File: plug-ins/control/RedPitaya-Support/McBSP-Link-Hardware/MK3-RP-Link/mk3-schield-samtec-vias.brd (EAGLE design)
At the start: 59.4 x 51.2 mm, 16 parts, among them U1 SN65MLVD202A, U2 SN65MLVD202A, U3 SN65MLVD202A

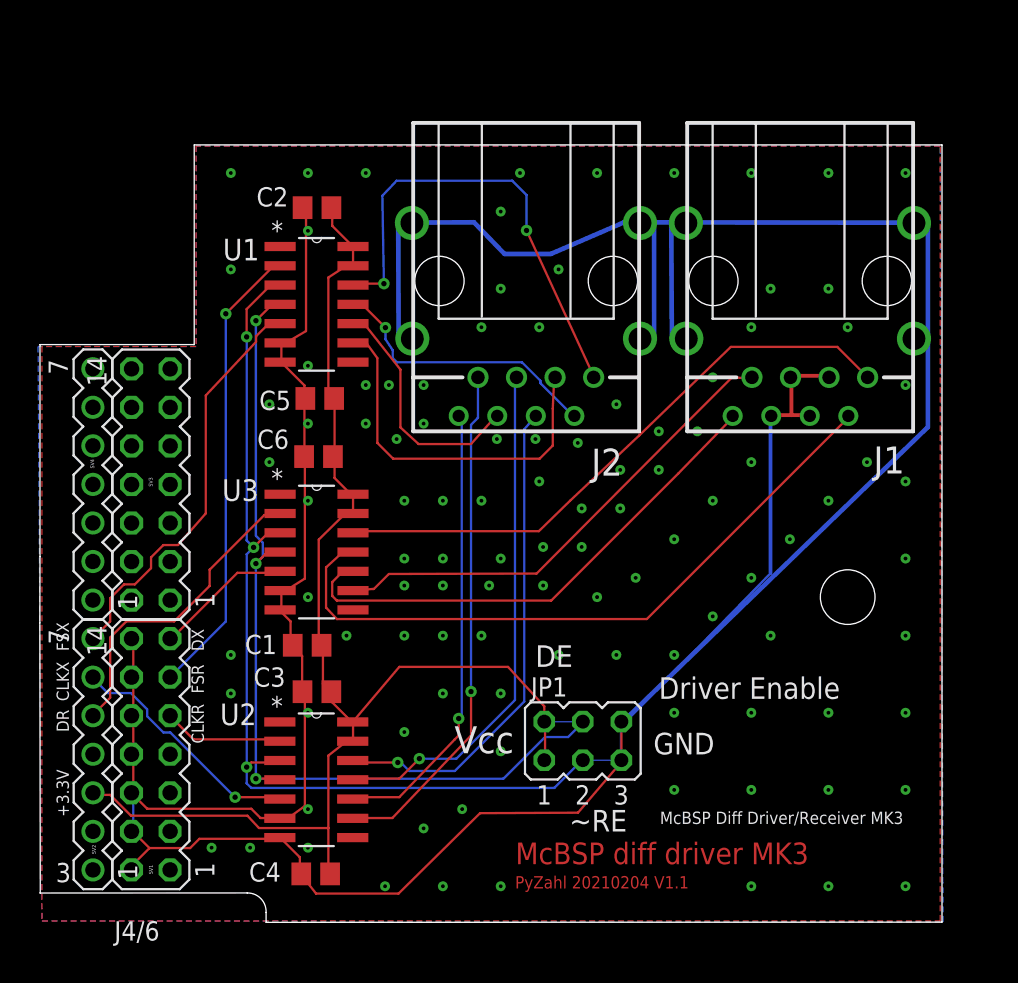
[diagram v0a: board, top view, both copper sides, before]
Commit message: added next version and support material
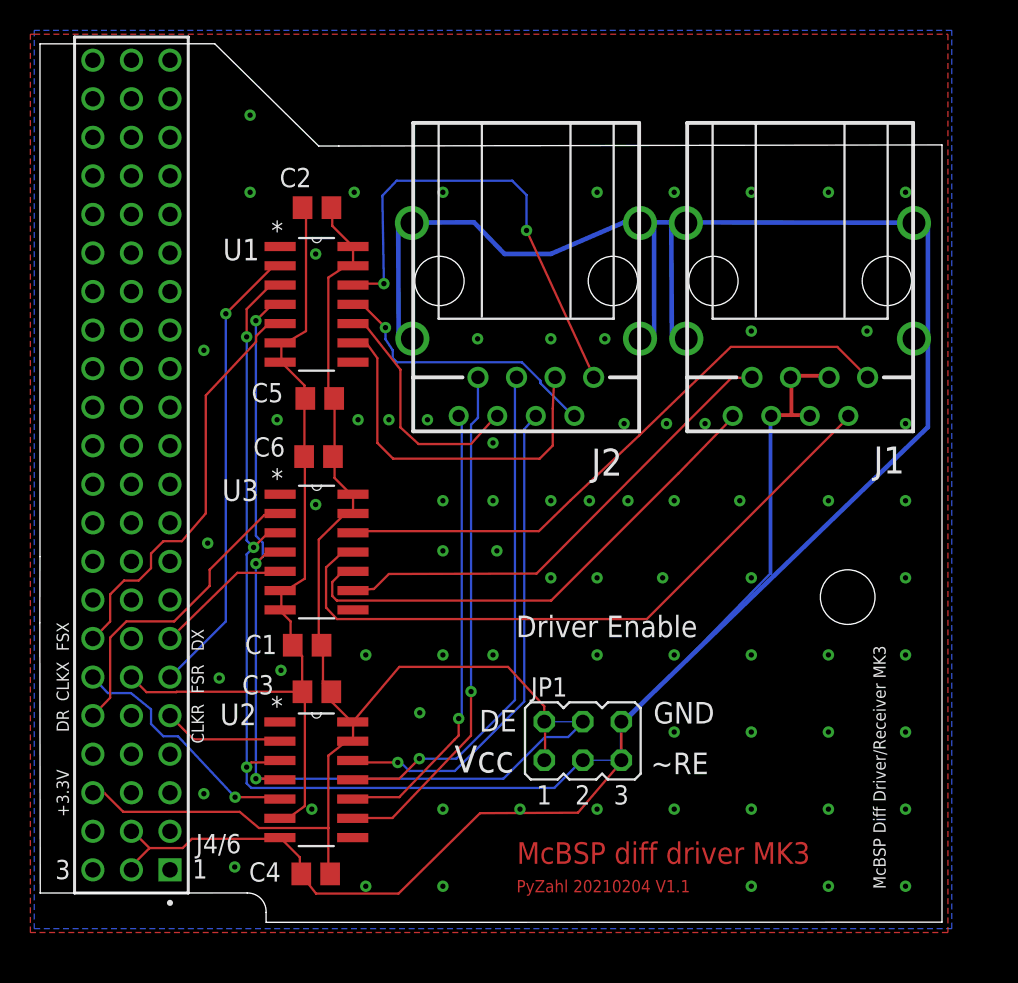
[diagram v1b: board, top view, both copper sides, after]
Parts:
- removed SV1, SV3: J4, con-lstb:MA07-2
- removed SV2, SV4: (no value), con-lstb-copy:MA07-1
- added J4/6: ESQ-122-13-L-T, ESQ-122-13-L-T:SAMTEC_ESQ-122-13-L-T
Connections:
- net CLKR0: now also J4/6.13; no longer SV1.9
- net CLKX0: now also J4/6.18; no longer SV2.6
- net DR0: now also J4/6.15; no longer SV2.5
- net DX0: now also J4/6.19; no longer SV1.13
- net FSR0: now also J4/6.16; no longer SV1.11
- net FSX0: now also J4/6.21; no longer SV2.7
- net GND: now also J4/6.02, J4/6.05, J4/6.08, J4/6.11, J4/6.14, J4/6.17, J4/6.20, J4/6.23, J4/6.26, J4/6.29, J4/6.32, J4/6.35, J4/6.38, J4/6.41, J4/6.44, J4/6.47, J4/6.50, J4/6.53, J4/6.56, J4/6.59, J4/6.62, J4/6.65; no longer SV1.10, SV1.12, SV1.14, SV1.2, SV1.4, SV1.6, SV1.8
- net VCC+3.3V: now also J4/6.09; no longer SV2.3
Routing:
- net GND: track 253.3 -> 241.0 mm, vias 0 -> 73
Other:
- board size 59.4 x 51.2 mm -> 59.4 x 57.9 mm
- board text added: "1"
- board text removed: "J4/6"

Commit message: updated McBSP Link board/schematics updated FPGA bit file for (latest build for V2 Hardware/Interface), design cleanups
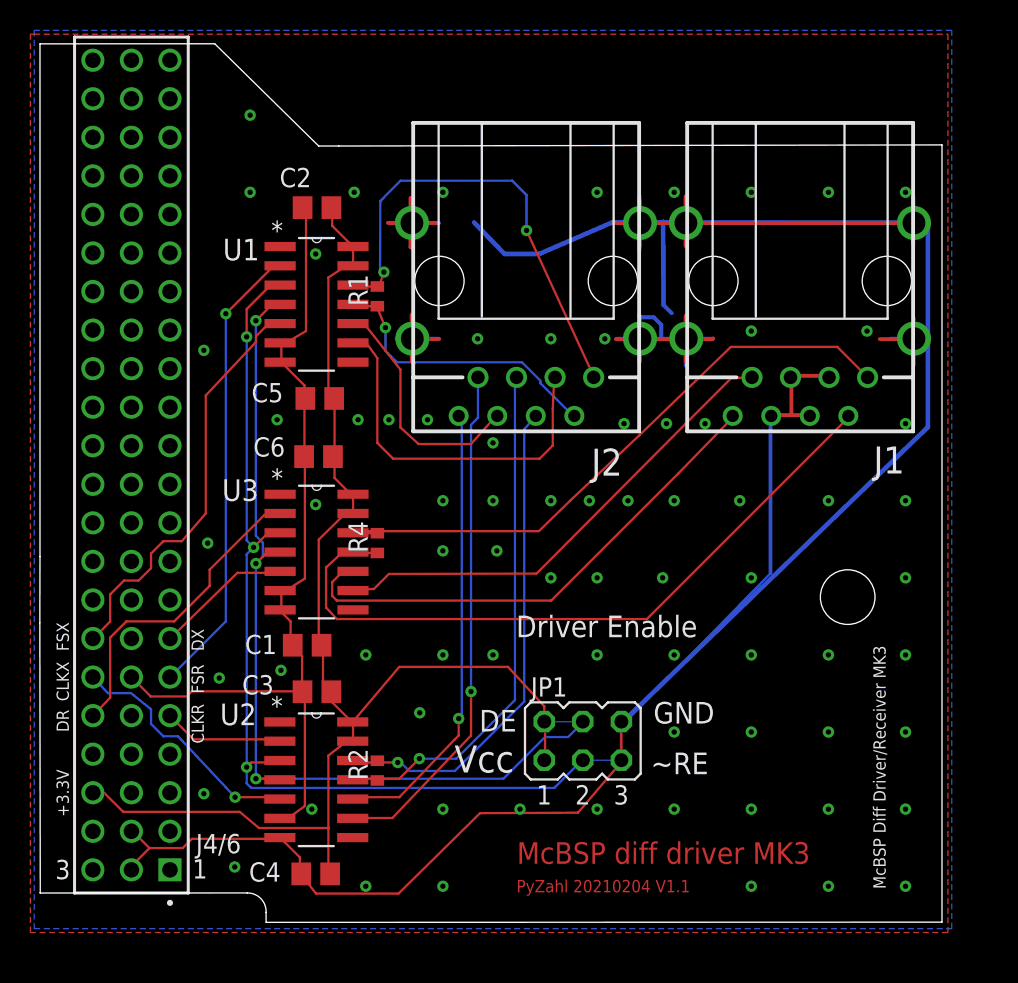
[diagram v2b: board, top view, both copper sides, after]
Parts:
- added R1, R2, R4: 100R, resistor:R0402
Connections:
- net N$1: now also R4.2
- net N$10: now also R2.1
- net N$2: now also R4.1
- net N$5: now also R1.2
- net N$6: now also R1.1
- net N$9: now also R2.2
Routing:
- net GND: track 241.0 -> 314.8 mm
- net N$2: track 45.3 -> 46.9 mm
- net N$1: track 39.7 -> 41.3 mm
- net N$6: track 18.5 -> 19.3 mm

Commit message: minor updates, cleanups
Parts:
- moved R1 0.11 mm to (23.7, 44.0)
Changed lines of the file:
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@@
 <drawing>
 <settings>
-<setting alwaysvectorfont="no"/>
+<setting alwaysvectorfont="yes"/>
 <setting verticaltext="up"/>
 </settings>
-<grid distance="10" unitdist="mil" unit="mil" style="dots" multiple="1" display="yes" altdistance="0.000123031496" altunitdist="mil" altunit="mil"/>
+<grid distance="0.000123031496" unitdist="mil" unit="mil" style="dots" multiple="1" display="no" altdistance="0.000123031496" altunitdist="mil" altunit="mil"/>
 <layers>
 <layer number="1" name="Top" color="4" fill="1" visible="yes" active="yes"/>
@@
 <attribute name="VALUE" x="12.78513125" y="46.712875" size="1.27" layer="27" rot="R90"/>
 </element>
-<element name="R4" library="resistor" library_urn="urn:adsk.eagle:library:348" package="R0402" package3d_urn="urn:adsk.eagle:package:26058/1" value="100R" x="23.622" y="27.686" rot="R90"/>
-<element name="R1" library="resistor" library_urn="urn:adsk.eagle:library:348" package="R0402" package3d_urn="urn:adsk.eagle:package:26058/1" value="100R" x="23.622" y="43.942" rot="R90"/>
-<element name="R2" library="resistor" library_urn="urn:adsk.eagle:library:348" package="R0402" package3d_urn="urn:adsk.eagle:package:26058/1" value="100R" x="23.622" y="12.7" rot="R90"/>
+<element name="R4" library="resistor" library_urn="urn:adsk.eagle:library:348" package="R0402" package3d_urn="urn:adsk.eagle:package:26058/1" value="100R" x="23.65425625" y="27.71019375" rot="R90"/>
+<element name="R1" library="resistor" library_urn="urn:adsk.eagle:library:348" package="R0402" package3d_urn="urn:adsk.eagle:package:26058/1" value="100R" x="23.703290625" y="44.0233" rot="R90"/>
+<element name="R2" library="resistor" library_urn="urn:adsk.eagle:library:348" package="R0402" package3d_urn="urn:adsk.eagle:package:26058/1" value="100R" x="23.61266875" y="12.73733125" rot="R90"/>
 </elements>
 <signals>
@@
 <wire x1="55.8546" y1="38.6842" x2="55.922" y2="38.607" width="0.1524" layer="1"/>
 <contactref element="R4" pad="2"/>
-<wire x1="23.622" y1="28.336" x2="22.048" y2="28.336" width="0.1524" layer="1"/>
+<wire x1="23.65425625" y1="28.36019375" x2="22.048" y2="28.336" width="0.1524" layer="1"/>
 <wire x1="22.048" y1="28.336" x2="22.017" y2="28.367" width="0.1524" layer="1"/>
 </signal>
@@
 <wire x1="54.6354" y1="35.941" x2="54.652" y2="36.067" width="0.1524" layer="1"/>
 <contactref element="R4" pad="1"/>
-<wire x1="23.622" y1="27.036" x2="22.078" y2="27.036" width="0.1524" layer="1"/>
+<wire x1="23.65425625" y1="27.06019375" x2="22.078" y2="27.036" width="0.1524" layer="1"/>
 <wire x1="22.078" y1="27.036" x2="22.017" y2="27.097" width="0.1524" layer="1"/>
 </signal>
@@
 <wire x1="23.48" y1="44.592" x2="22.112" y2="44.592" width="0.1524" layer="1"/>
 <wire x1="22.112" y1="44.592" x2="22.017" y2="44.687" width="0.1524" layer="1"/>
-<wire x1="23.622" y1="44.592" x2="23.48" y2="44.592" width="0.1524" layer="1"/>
+<wire x1="23.703290625" y1="44.6733" x2="23.48" y2="44.592" width="0.1524" layer="1"/>
 <wire x1="23.48" y1="44.592" x2="23.7998" y2="44.7802" width="0.1524" layer="1"/>
 </signal>
@@
 <via x="24.1554" y="41.8846" extent="1-16" drill="0.35"/>
 <contactref element="R1" pad="1"/>
-<wire x1="23.622" y1="43.292" x2="23.256" y2="43.292" width="0.1524" layer="1"/>
+<wire x1="23.703290625" y1="43.3733" x2="23.256" y2="43.292" width="0.1524" layer="1"/>
 </signal>
 <signal name="N$7">
@@
 <via x="24.9682" y="13.2334" extent="1-16" drill="0.35"/>
 <contactref element="R2" pad="2"/>
-<wire x1="24.9682" y1="13.2334" x2="23.622" y2="13.35" width="0" layer="19" extent="1-16"/>
+<wire x1="24.9682" y1="13.2334" x2="23.61266875" y2="13.38733125" width="0" layer="19" extent="1-16"/>
 </signal>
 <signal name="N$10">
@@
 <via x="26.3906" y="13.4874" extent="1-16" drill="0.35"/>
 <contactref element="R2" pad="1"/>
-<wire x1="25.0698" y1="12.1666" x2="23.622" y2="12.05" width="0" layer="19" extent="1-1"/>
+<wire x1="25.0698" y1="12.1666" x2="23.61266875" y2="12.08733125" width="0" layer="19" extent="1-1"/>
 </signal>
 <signal name="N$11">

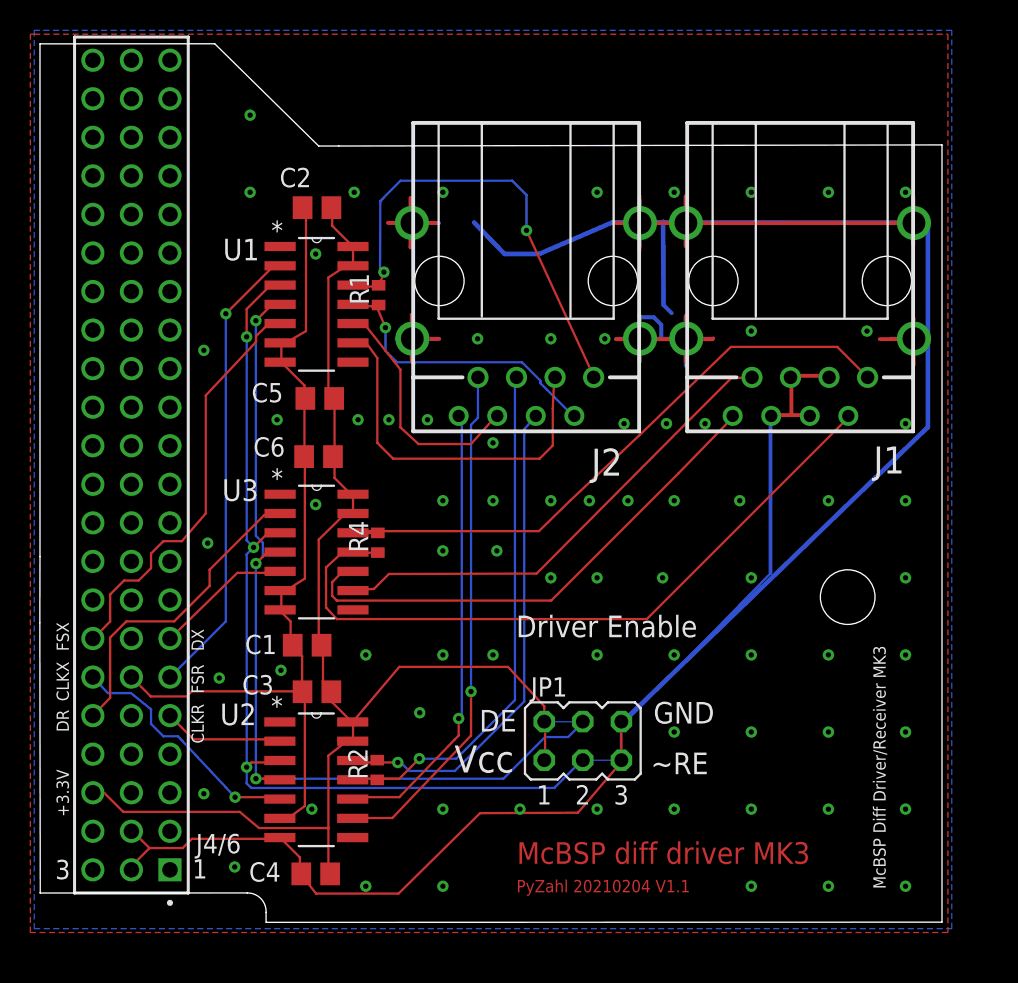
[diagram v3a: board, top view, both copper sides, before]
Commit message: updated FPGA init procedure updated -- next gen layout
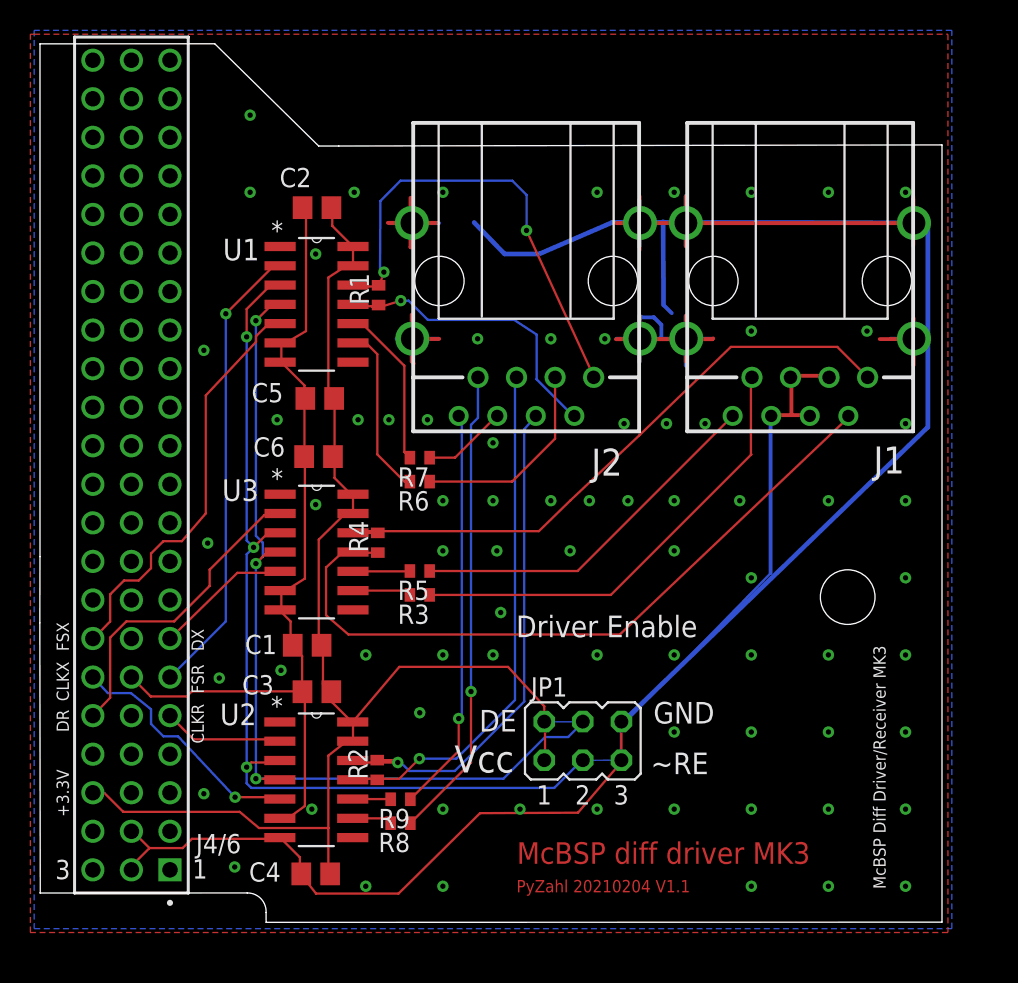
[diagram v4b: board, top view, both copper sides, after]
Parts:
- added R3, R5, R6, R7, R8, R9: 25R, resistor:R0402
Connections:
- new net N$13: R3.2, U3.9
- new net N$14: R5.2, U3.10
- new net N$15: R6.2, U1.9
- new net N$16: R7.2, U1.10
- new net N$17: R8.2, U2.9
- new net N$18: R9.2, U2.10
- net N$11: now also R8.1; no longer U2.9
- net N$12: now also R9.1; no longer U2.10
- net N$3: now also R3.1; no longer U3.9
- net N$4: now also R5.1; no longer U3.10
- net N$7: now also R6.1; no longer U1.9
- net N$8: now also R7.1; no longer U1.10
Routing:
- net N$15: track 0.00 -> 11.4 mm
- net N$7: track 24.7 -> 13.5 mm
- net N$16: track 0.00 -> 10.7 mm
- net N$8: track 16.1 -> 5.64 mm
- net N$4: track 34.3 -> 24.3 mm
- net N$13: track 0.00 -> 3.87 mm
- net N$14: track 0.00 -> 3.76 mm
- net N$12: track 30.2 -> 26.9 mm
- net N$11: track 33.9 -> 31.2 mm
- net N$17: track 0.00 -> 2.63 mm
- net N$18: track 0.00 -> 2.50 mm
- net N$3: track 32.1 -> 30.1 mm
- net N$9: track 32.6 -> 34.1 mm
- net N$2: track 46.9 -> 47.8 mm
- net N$6: track 19.4 -> 19.9 mm
